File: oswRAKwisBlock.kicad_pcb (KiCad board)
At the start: 2 copper layers, 33.8 x 46 mm, 0 parts

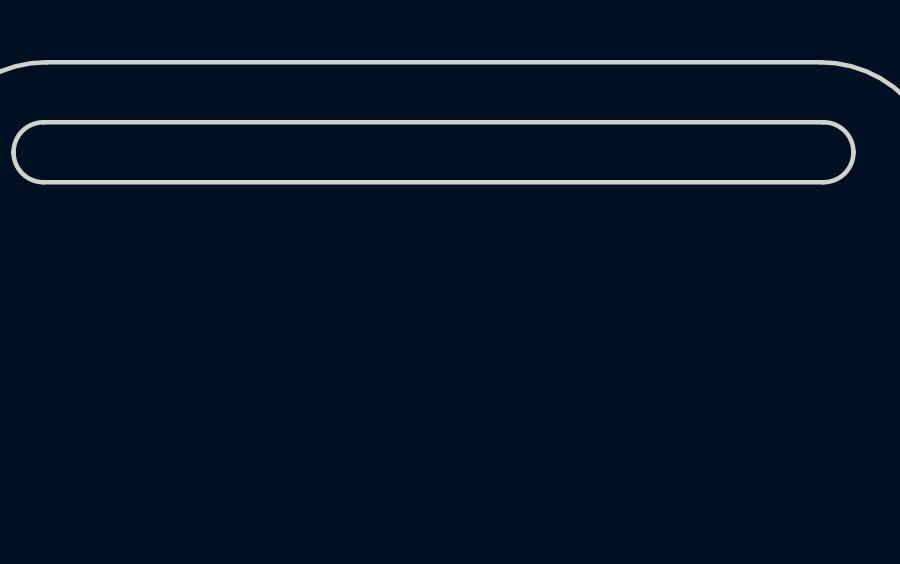
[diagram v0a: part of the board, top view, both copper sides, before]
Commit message: Adding connector.
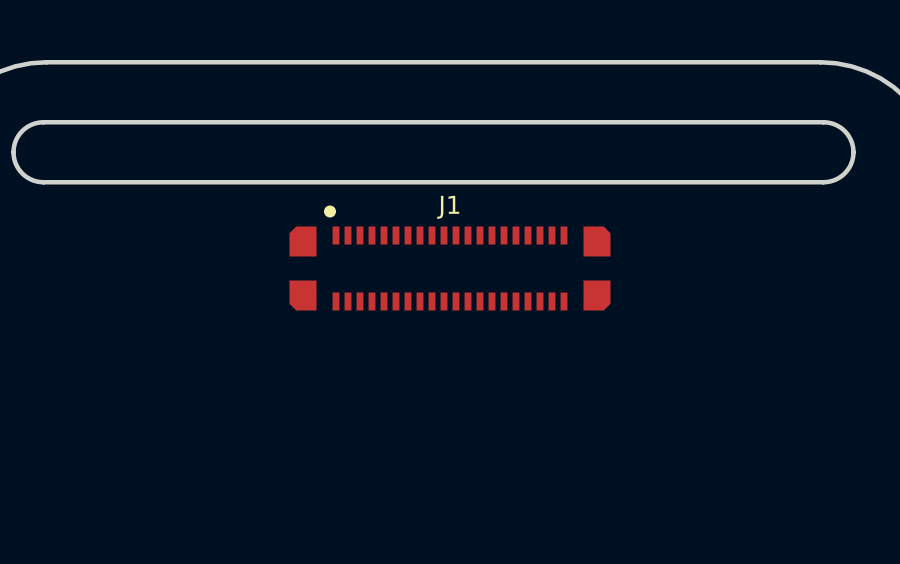
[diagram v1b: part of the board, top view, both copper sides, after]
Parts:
- added J1: WisBlock, AllardConnFootPrints:TXGA_FBB04004-F40S1003K6M, F.Cu at (137.3, 106.9)

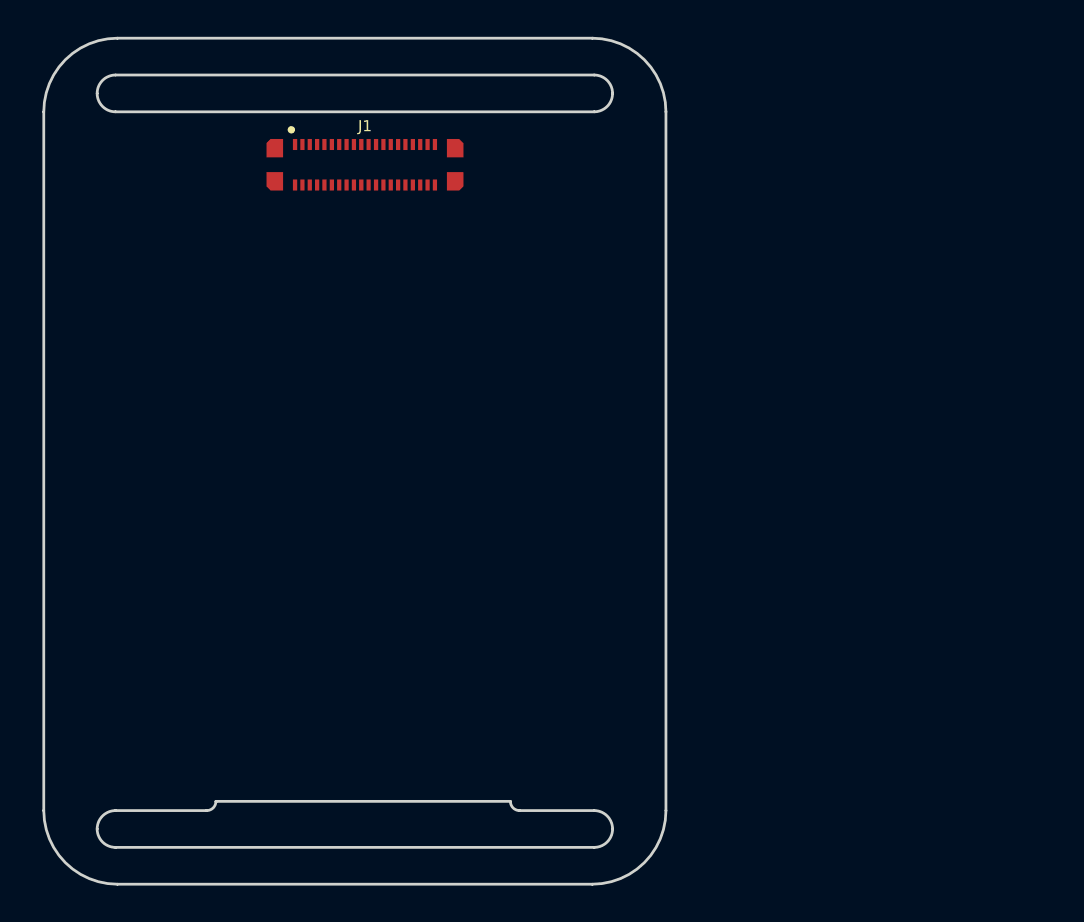
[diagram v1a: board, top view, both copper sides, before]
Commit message: Getting the wisblock footprint on the board.
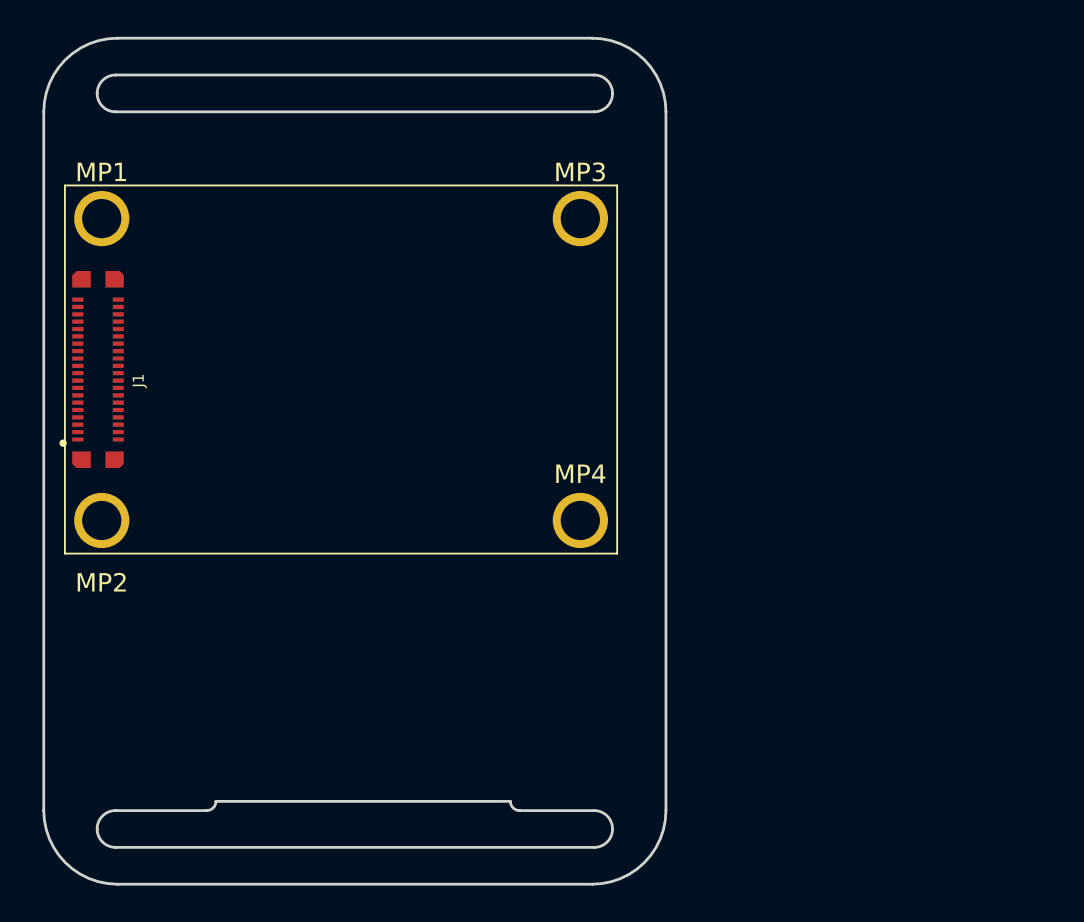
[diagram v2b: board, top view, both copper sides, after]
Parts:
- added MP1: M3 1mm, AllardMountingHW:MTGNP300H213Z565, F.Cu at (123.0, 109.8)
- added MP2: M3 1mm, AllardMountingHW:MTGNP300H213Z565, F.Cu at (123.0, 126.2)
- added MP3: M3 1mm, AllardMountingHW:MTGNP300H213Z565, F.Cu at (149.0, 109.8)
- added MP4: M3 1mm, AllardMountingHW:MTGNP300H213Z565, F.Cu at (149.0, 126.2)
- moved J1 18.3 mm to (122.8, 118.0), turned to 90 degrees

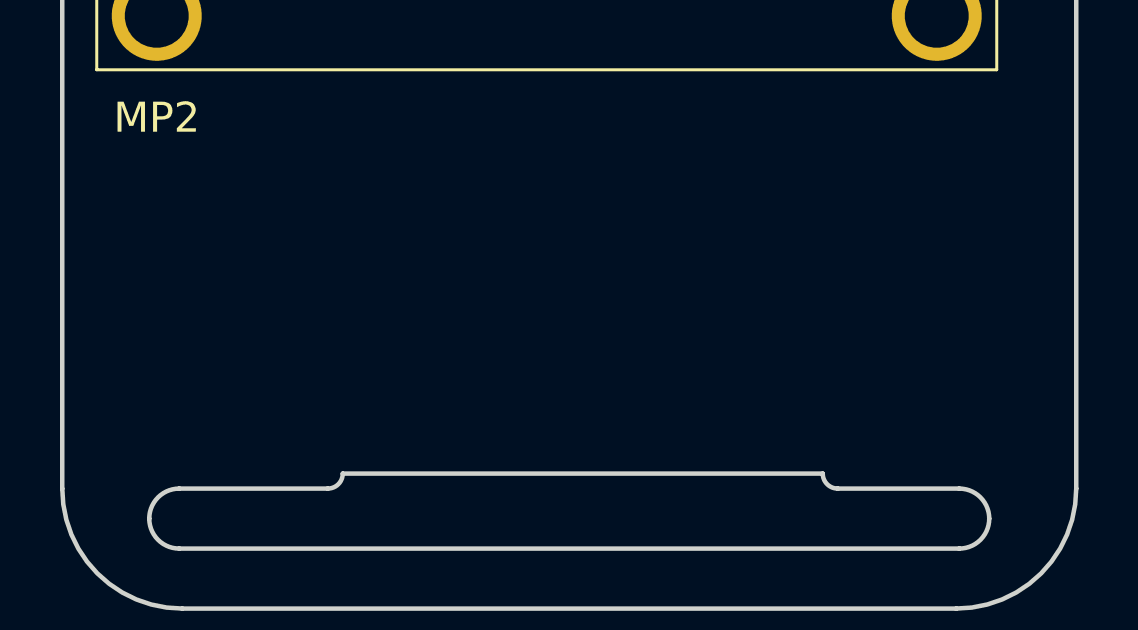
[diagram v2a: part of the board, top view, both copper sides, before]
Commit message: Adding the FPs to the board.
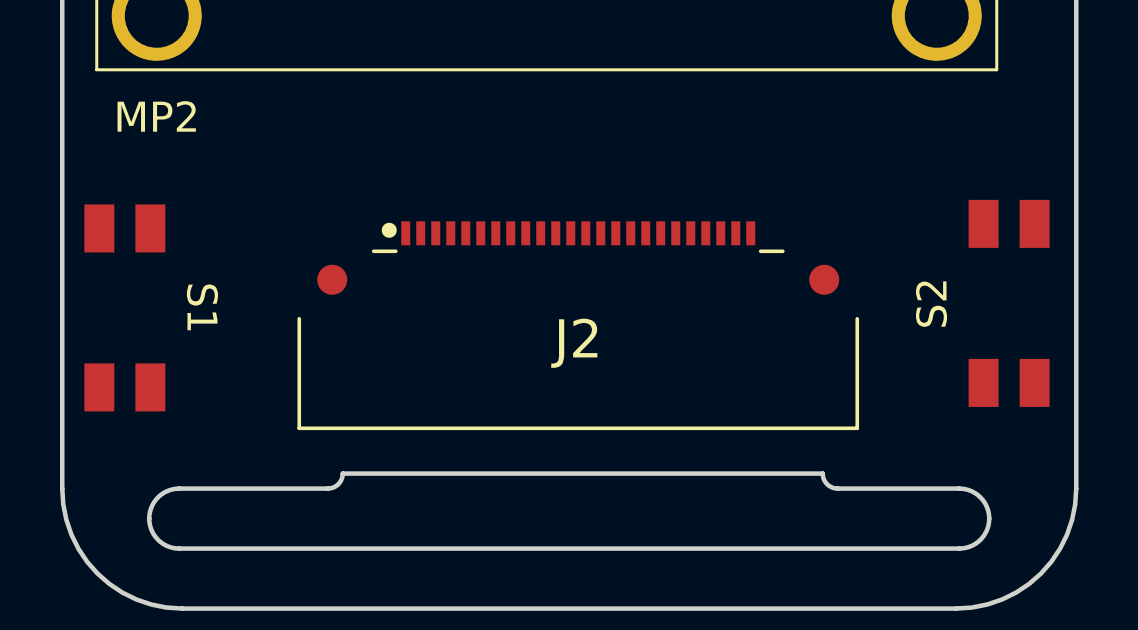
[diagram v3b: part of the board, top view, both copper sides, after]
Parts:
- added J2: 0524352471, AllardConnFootPrints:MOLEX_52435-2471, F.Cu at (137.1, 137.0)
- added S1: tactile_sw, AllardSpecialFootPrints:Panasonic_EVQPUA02K, F.Cu at (121.9, 135.9)
- added S2: tactile_sw, AllardSpecialFootPrints:Panasonic_EVQPUA02K, F.Cu at (151.4, 135.8)

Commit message: Updates.
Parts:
- added R1: 10k, AllardChip:RESC40X20X15L10N, F.Cu at (134.2, 130.2)
- added R2: 10k, AllardChip:RESC40X20X15L10N, F.Cu at (136.0, 130.2)
- added R3: 10k, AllardChip:RESC40X20X15L10N, F.Cu at (120.8, 119.2)
- moved J1 0.86 mm to (123.3, 117.3)
- moved MP1 0.86 mm to (123.5, 109.1)
- moved MP2 0.86 mm to (123.5, 125.5)
- moved MP3 0.86 mm to (149.5, 109.1)
- moved MP4 0.86 mm to (149.5, 125.5)
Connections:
- J1 pad 13: unconnected-(J1-RESET-Pad13) -> Net-(J1-RESET)
- J1 pad 39: unconnected-(J1-FS3-Pad39) -> GND
- J1 pad 40: unconnected-(J1-GND-Pad40) -> GND
- J1 pad 5: unconnected-(J1-3V3-Pad5) -> VDD
- J1 pad FS1: unconnected-(J1-GND-PadFS1) -> GND
- J1 pad FS2: unconnected-(J1-GND-PadFS2) -> GND
- J1 pad FS4: unconnected-(J1-GND-PadFS4) -> GND
- S1 pad 1: unconnected-(S1-Pad1) -> Net-(R1-Pad2)
- S1 pad 2: unconnected-(S1-Pad2) -> Net-(R1-Pad2)
- S1 pad 3: unconnected-(S1-K-Pad3) -> GND
- S1 pad 4: unconnected-(S1-A-Pad4) -> GND
- S2 pad 1: unconnected-(S2-Pad1) -> Net-(R2-Pad2)
- S2 pad 2: unconnected-(S2-Pad2) -> Net-(R2-Pad2)
- S2 pad 3: unconnected-(S2-K-Pad3) -> GND
- S2 pad 4: unconnected-(S2-A-Pad4) -> GND

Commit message: Working forward.
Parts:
- added Q1: SI1308EDL-T1-GE3, AllardSOT:SOT23-3P65_210X110L20X32N, F.Cu at (131.7, 132.6)
- added REF**: SIMCOM_SIM68M, AllardSpecialFootPrints:SIMCOM_SIM68M, F.Cu at (143.7, 129.7)
- added REF**: MOLEX_2169890001, AllardConnFootPrints:MOLEX_2169890001, F.Cu at (119.8, 127.6)
- added U1: MCP73811T-420I/OT, AllardSOT:SOT23-5P95_270X145L35X35N, F.Cu at (128.3, 133.1)
- moved MP3 3.01 mm to (149.8, 106.1)
- moved MP4 3.01 mm to (149.8, 122.5)
- moved J1 3.01 mm to (123.6, 114.3)
- moved MP1 3.01 mm to (123.8, 106.1)
- moved MP2 3.01 mm to (123.8, 122.5)
- moved J2 2.20 mm to (136.9, 139.2)
- moved S1 1.99 mm to (121.6, 137.9)
- moved S2 0.45 mm to (151.9, 135.8)

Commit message: Updates.
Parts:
- removed the REF** at (119.8, 127.6)
- added J3: USB_B_Micro, AllardConnFootPrints:MOLEX_1051330011, F.Cu at (122.4, 127.4)
- moved R3 4.71 mm to (121.1, 114.5)
- moved J1 2.00 mm to (123.6, 112.3)
- moved MP1 2.00 mm to (123.8, 104.1)
- moved MP2 2.00 mm to (123.8, 120.5)
- moved MP3 2.00 mm to (149.8, 104.1)
- moved MP4 2.00 mm to (149.8, 120.5)
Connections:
- J1 pad 7: unconnected-(J1-USB+-Pad7) -> /USB_+
- J1 pad 8: unconnected-(J1-USB--Pad8) -> /USB_-
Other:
- outline, holes or cut-outs redrawn

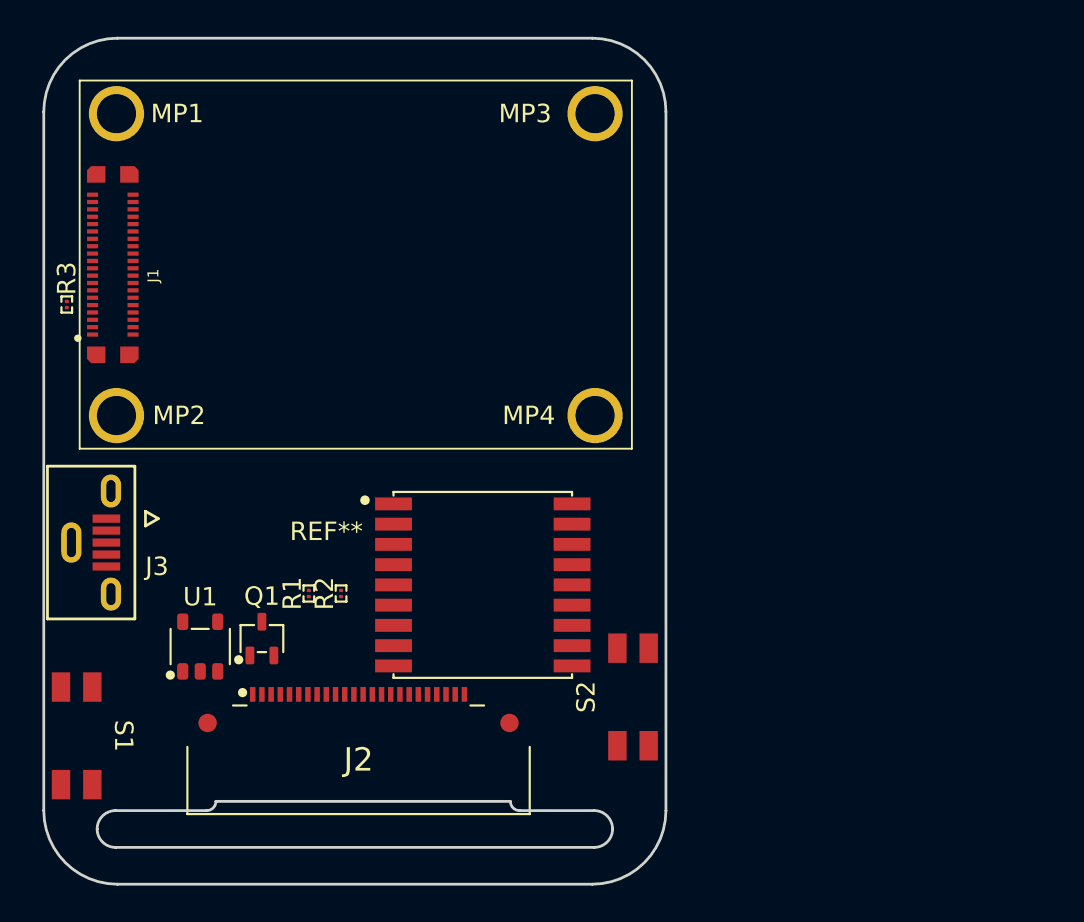
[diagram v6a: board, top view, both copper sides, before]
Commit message: Updating the board and moving some things around.
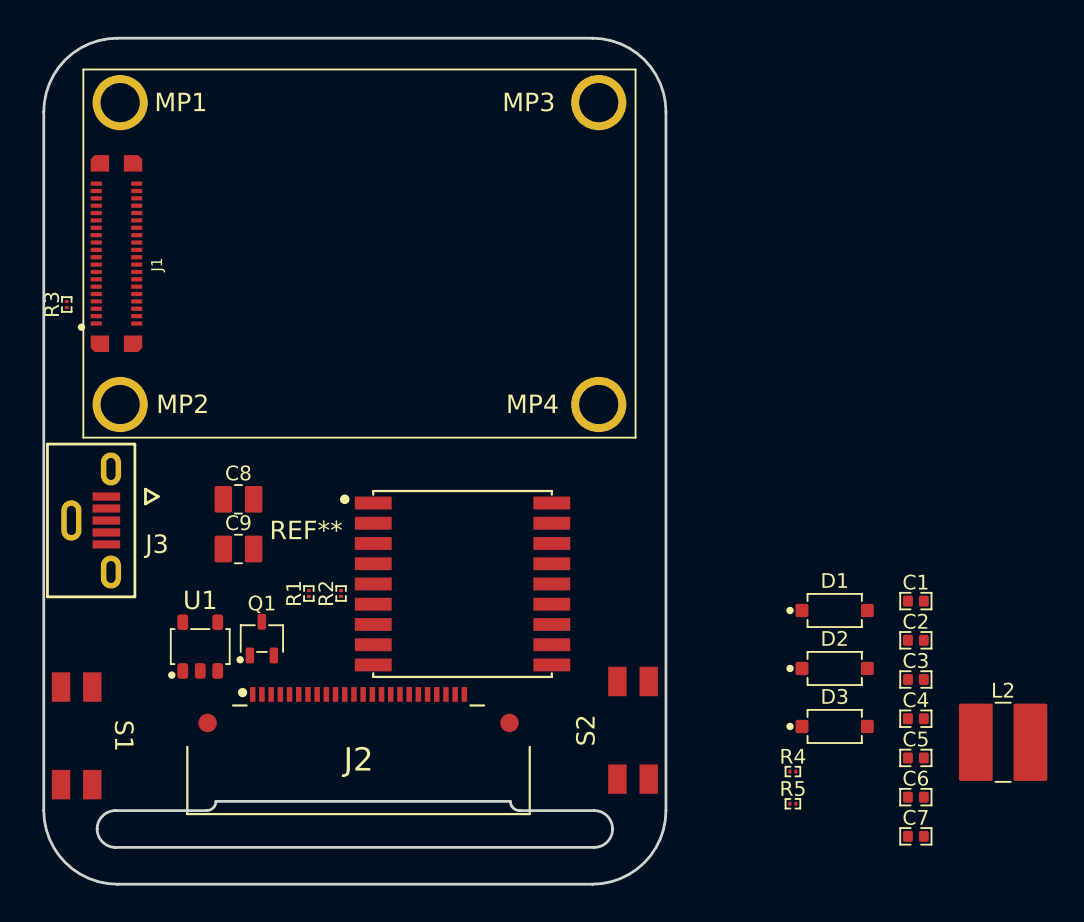
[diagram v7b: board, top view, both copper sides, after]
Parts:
- added C1: 1u, AllardChip:CAPC100X50X60L25L, F.Cu at (167.2, 130.6)
- added C2: 1u, AllardChip:CAPC100X50X60L25L, F.Cu at (167.2, 132.7)
- added C3: 1u, AllardChip:CAPC100X50X60L25L, F.Cu at (167.2, 134.8)
- added C4: 1u, AllardChip:CAPC100X50X60L25L, F.Cu at (167.2, 137.0)
- added C5: 1u, AllardChip:CAPC100X50X60L25L, F.Cu at (167.2, 139.1)
- added C6: 1u, AllardChip:CAPC100X50X60L25L, F.Cu at (167.2, 141.2)
- added C7: 1u, AllardChip:CAPC100X50X60L25L, F.Cu at (167.2, 143.4)
- added C8: 4.7u, AllardChip:CAPC200X125X145L45L, F.Cu at (130.4, 125.0)
- added C9: 4.7u, AllardChip:CAPC200X125X145L45L, F.Cu at (130.4, 127.8)
- added D1: MBR0540T1G, AllardSOD:SOD370X155X135L32X57L, F.Cu at (162.8, 131.1)
- added D2: MBR0540T1G, AllardSOD:SOD370X155X135L32X57L, F.Cu at (162.8, 134.2)
- added D3: MBR0540T1G, AllardSOD:SOD370X155X135L32X57L, F.Cu at (162.8, 137.4)
- added L2: 10u, AllardChip:INDC400X400X120L120L, F.Cu at (172.0, 138.2)
- added R4: 100k, AllardChip:RESC40X20X15L10L, F.Cu at (160.5, 139.8)
- added R5: 10k, AllardChip:RESC40X20X15L10L, F.Cu at (160.5, 141.6)
- Q1: footprint AllardSOT:SOT23-3P65_210X110L20X32N -> AllardSOT:SOT23-3P65_210X110L20X32L
- R1, R2, R3: footprint AllardChip:RESC40X20X15L10N -> AllardChip:RESC40X20X15L10L
- U1: footprint AllardSOT:SOT23-5P95_270X145L35X35N -> AllardSOT:SOT23-5P95_270X145L35X35L
- moved S2 1.81 mm to (151.9, 137.6)
- moved J3 1.20 mm to (122.4, 126.2)
- moved REF** 1.10 mm to (142.6, 129.7)
- moved J1 0.63 mm to (123.8, 111.7)
- moved MP1 0.63 mm to (124.0, 103.5)
- moved MP2 0.63 mm to (124.0, 119.9)
- moved MP3 0.63 mm to (150.0, 103.5)
- moved MP4 0.63 mm to (150.0, 119.9)
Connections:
- J2 pad 18: unconnected-(J2-Pin_18-Pad18) -> Net-(J2-Pin_18)
- J2 pad 20: unconnected-(J2-Pin_20-Pad20) -> Net-(J2-Pin_20)
- J2 pad 22: unconnected-(J2-Pin_22-Pad22) -> Net-(J2-Pin_22)
- J2 pad 24: unconnected-(J2-Pin_24-Pad24) -> Net-(J2-Pin_24)
- J2 pad 3: /~{RESET} -> GND
- J2 pad 5: unconnected-(J2-Pin_5-Pad5) -> Net-(J2-Pin_5)
- J3 pad 5: unconnected-(J3-GND-Pad5) -> GND
- J3 pad 6: (no net) -> unconnected-(J3-Shield-Pad6)
- Q1 pad 1: unconnected-(Q1-G-Pad1) -> /GDR
- Q1 pad 2: unconnected-(Q1-S-Pad2) -> GND
- Q1 pad 3: unconnected-(Q1-D-Pad3) -> Net-(D3-A)

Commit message: Working on it....
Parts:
- added C10: 1u, AllardChip:CAPC100X50X60L25L, F.Cu at (122.5, 122.8)
- D1, D2, D3: footprint AllardSOD:SOD370X155X135L32X57L -> AllardSOD:SOD370X155X135L32X57N
- moved L2 44.5 mm to (127.8, 133.1), turned to 90 degrees
- moved C6 34.0 mm to (133.9, 134.4)
- moved C5 30.5 mm to (137.2, 133.9), turned to 90 degrees
- moved R5 29.4 mm to (132.0, 134.6)
- moved C4 29.0 mm to (138.3, 134.0), turned to 90 degrees
- moved C7 28.8 mm to (140.3, 133.2), turned to 180 degrees
- moved C3 27.4 mm to (139.8, 134.3), turned to 180 degrees
- moved C2 25.6 mm to (141.7, 133.9), turned to 90 degrees
- moved R4 25.4 mm to (135.7, 134.4), turned to -90 degrees
- moved D3 24.7 mm to (138.8, 131.6), turned to 180 degrees
- moved D2 24.5 mm to (138.8, 129.4), turned to 180 degrees
- moved D1 24.3 mm to (138.8, 127.2)
- moved C1 23.6 mm to (144.1, 135.1)
- moved R2 15.3 mm to (151.0, 133.2), turned to -90 degrees
- moved R1 14.0 mm to (124.8, 140.4), turned to 180 degrees
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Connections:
- C9 pad 1: Net-(D1-K) -> Net-(C9-Pad1)
- C9 pad 2: Net-(D3-A) -> Net-(D3-K)
- D1 pad A: (no net) -> /PREVGL
- D1 pad C: (no net) -> Net-(C9-Pad1)
- D2 pad A: (no net) -> Net-(C9-Pad1)
- D2 pad C: (no net) -> GND
- D3 pad A: (no net) -> Net-(D3-K)
- D3 pad C: (no net) -> /PREVGH
- J3 pad 1: unconnected-(J3-VBUS-Pad1) -> VUSB_BUS
- L2 pad 2: Net-(D3-A) -> Net-(D3-K)
- Q1 pad 3: Net-(D3-A) -> Net-(D3-K)
- R1 pad 2: Net-(R1-Pad2) -> Net-(S1-K)
- R2 pad 2: Net-(R2-Pad2) -> Net-(S2-K)
- S1 pad 1: Net-(R1-Pad2) -> Net-(S1-K)
- S1 pad 2: Net-(R1-Pad2) -> GND
- S1 pad 3: GND -> Net-(S1-K)
- S2 pad 1: Net-(R2-Pad2) -> Net-(S2-K)
- S2 pad 2: Net-(R2-Pad2) -> GND
- S2 pad 3: GND -> Net-(S2-K)
- U1 pad 1: unconnected-(U1-CE-Pad1) -> VUSB_BUS
- U1 pad 2: unconnected-(U1-V_{SS}-Pad2) -> GND
- U1 pad 4: unconnected-(U1-V_{DD}-Pad4) -> VUSB_BUS
- U1 pad 5: unconnected-(U1-PROG-Pad5) -> VUSB_BUS
